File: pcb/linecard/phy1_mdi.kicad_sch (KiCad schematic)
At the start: 51 parts, among them J5 LPJT476156AENL, J9 LPJT476156AENL, U35 VSC8512, U36 ESD224DQAR, U37 ESD224DQAR, U38 ESD224DQAR, U39 ESD224DQAR, U40 ESD224DQAR, U41 ESD224DQAR, U42 ESD224DQAR, U43 ESD224DQAR, U44 ESD224DQAR, U45 ESD224DQAR, U46 ESD224DQAR, U47 ESD224DQAR, U48 ESD224DQAR, U49 ESD224DQAR, U50 ESD224DQAR, U51 ESD224DQAR, U52 ESD224DQAR, U53 ESD224DQAR, U54 ESD224DQAR, U55 ESD224DQAR, U56 ESD224DQAR, U57 ESD224DQAR, U58 ESD224DQAR, U59 ESD224DQAR

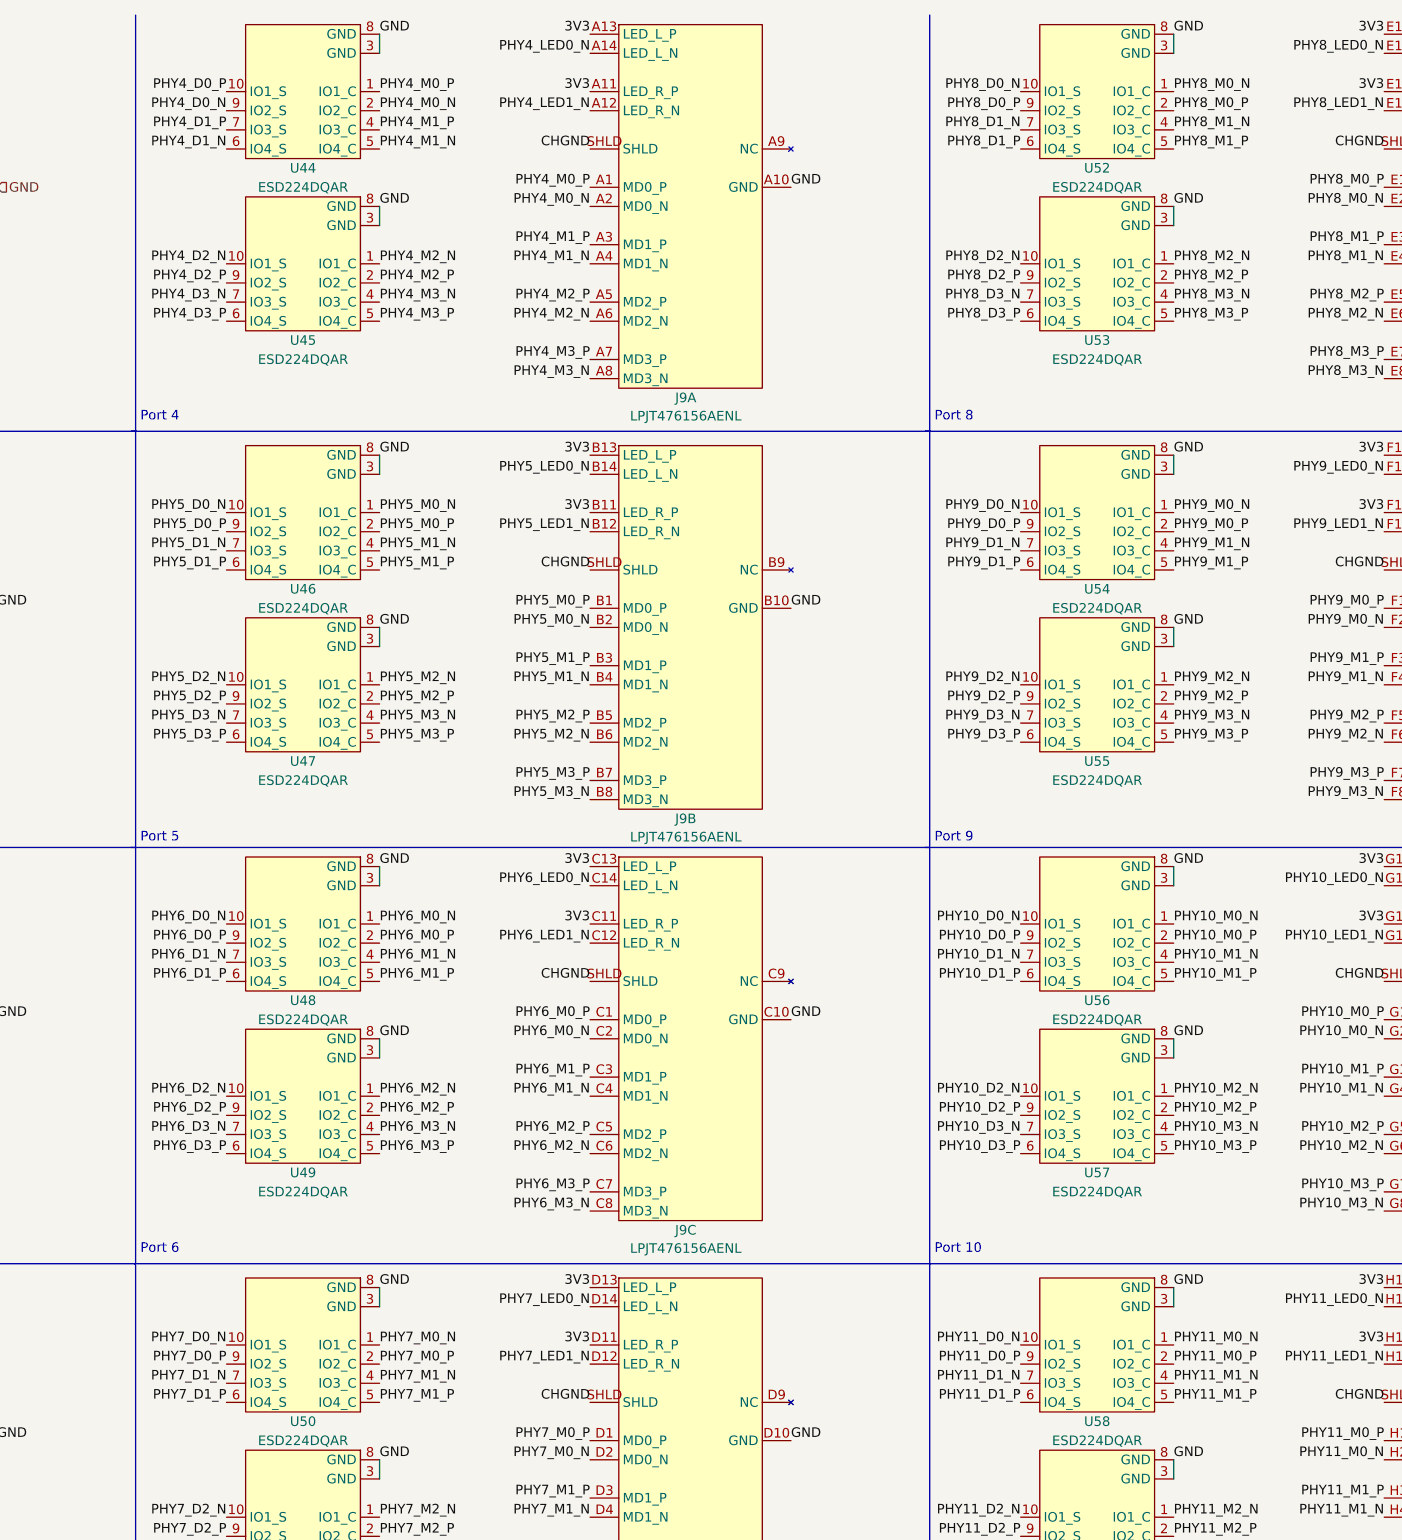
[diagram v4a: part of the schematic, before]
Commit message: 576 unrouted. More decoupling and baseT work on right side PHY. Started LED fanout.
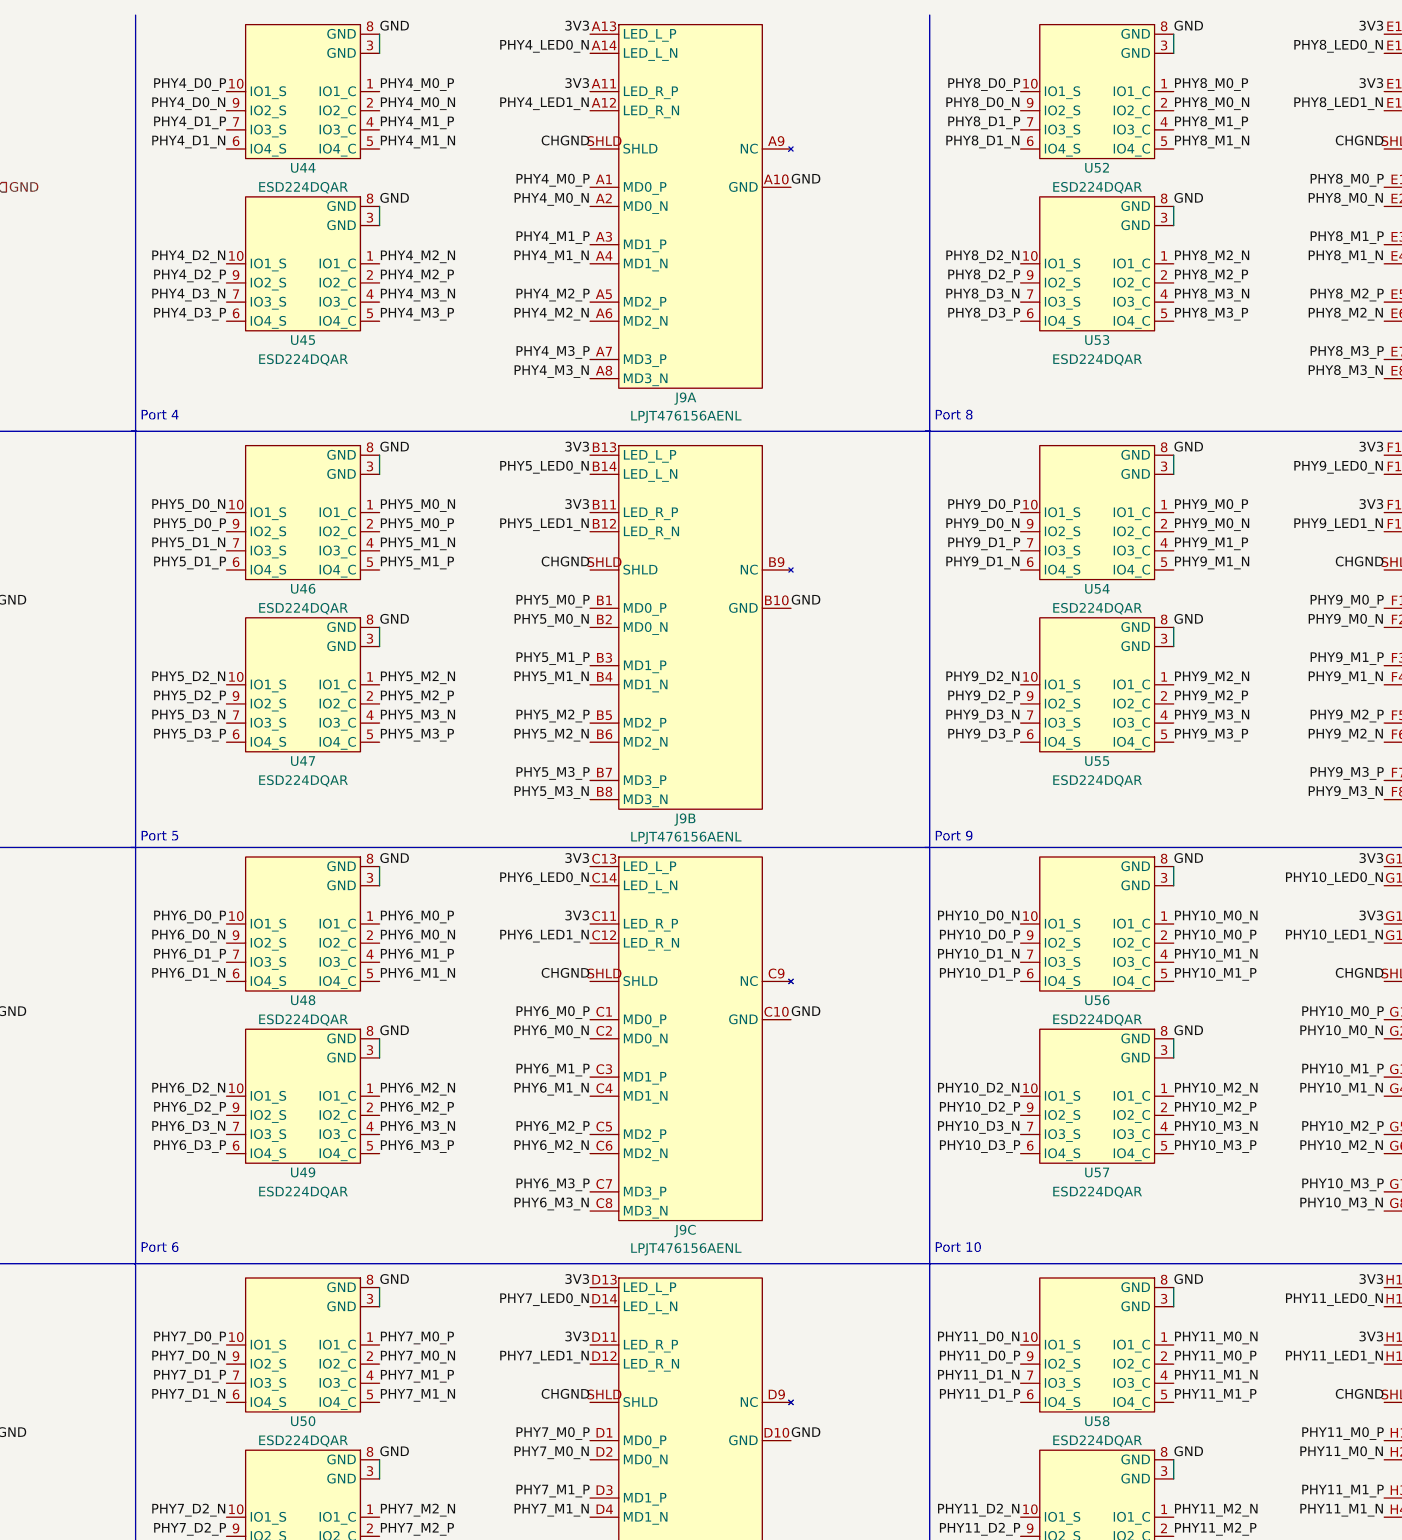
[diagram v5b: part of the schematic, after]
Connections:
- net PHY6_D0_N: now also U48.9 (IO2_S); no longer U48.10 (IO1_S)
- net PHY6_D0_P: now also U48.10 (IO1_S); no longer U48.9 (IO2_S)
- net PHY6_D1_N: now also U48.6 (IO4_S); no longer U48.7 (IO3_S)
- net PHY6_D1_P: now also U48.7 (IO3_S); no longer U48.6 (IO4_S)
- net PHY6_M0_N: now also U48.2 (IO2_C); no longer U48.1 (IO1_C)
- net PHY6_M0_P: now also U48.1 (IO1_C); no longer U48.2 (IO2_C)
- net PHY6_M1_N: now also U48.5 (IO4_C); no longer U48.4 (IO3_C)
- net PHY6_M1_P: now also U48.4 (IO3_C); no longer U48.5 (IO4_C)
- net PHY7_D0_N: now also U50.9 (IO2_S); no longer U50.10 (IO1_S)
- net PHY7_D0_P: now also U50.10 (IO1_S); no longer U50.9 (IO2_S)
- net PHY7_D1_N: now also U50.6 (IO4_S); no longer U50.7 (IO3_S)
- net PHY7_D1_P: now also U50.7 (IO3_S); no longer U50.6 (IO4_S)
- net PHY7_M0_N: now also U50.2 (IO2_C); no longer U50.1 (IO1_C)
- net PHY7_M0_P: now also U50.1 (IO1_C); no longer U50.2 (IO2_C)
- net PHY7_M1_N: now also U50.5 (IO4_C); no longer U50.4 (IO3_C)
- net PHY7_M1_P: now also U50.4 (IO3_C); no longer U50.5 (IO4_C)
- net PHY8_D0_N: now also U52.9 (IO2_S); no longer U52.10 (IO1_S)
- net PHY8_D0_P: now also U52.10 (IO1_S); no longer U52.9 (IO2_S)
- net PHY8_D1_N: now also U52.6 (IO4_S); no longer U52.7 (IO3_S)
- net PHY8_D1_P: now also U52.7 (IO3_S); no longer U52.6 (IO4_S)
- net PHY8_M0_N: now also U52.2 (IO2_C); no longer U52.1 (IO1_C)
- net PHY8_M0_P: now also U52.1 (IO1_C); no longer U52.2 (IO2_C)
- net PHY8_M1_N: now also U52.5 (IO4_C); no longer U52.4 (IO3_C)
- net PHY8_M1_P: now also U52.4 (IO3_C); no longer U52.5 (IO4_C)
- net PHY9_D0_N: now also U54.9 (IO2_S); no longer U54.10 (IO1_S)
- net PHY9_D0_P: now also U54.10 (IO1_S); no longer U54.9 (IO2_S)
- net PHY9_D1_N: now also U54.6 (IO4_S); no longer U54.7 (IO3_S)
- net PHY9_D1_P: now also U54.7 (IO3_S); no longer U54.6 (IO4_S)
- net PHY9_M0_N: now also U54.2 (IO2_C); no longer U54.1 (IO1_C)
- net PHY9_M0_P: now also U54.1 (IO1_C); no longer U54.2 (IO2_C)
- net PHY9_M1_N: now also U54.5 (IO4_C); no longer U54.4 (IO3_C)
- net PHY9_M1_P: now also U54.4 (IO3_C); no longer U54.5 (IO4_C)
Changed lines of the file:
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@@
 	)
 	(label "PHY6_M1_P"
-		(at 228.6 140.97 0)
+		(at 228.6 138.43 0)
 		(fields_autoplaced yes)
 		(effects
@@
 	)
 	(label "PHY8_D1_P"
-		(at 313.69 30.48 180)
+		(at 313.69 27.94 180)
 		(fields_autoplaced yes)
 		(effects
@@
 	)
 	(label "PHY8_D1_N"
-		(at 313.69 27.94 180)
+		(at 313.69 30.48 180)
 		(fields_autoplaced yes)
 		(effects
@@
 	)
 	(label "PHY9_M0_N"
-		(at 334.01 78.74 0)
+		(at 334.01 81.28 0)
 		(fields_autoplaced yes)
 		(effects
@@
 	)
 	(label "PHY7_D0_N"
-		(at 208.28 189.23 180)
+		(at 208.28 191.77 180)
 		(fields_autoplaced yes)
 		(effects
@@
 	)
 	(label "PHY7_D0_P"
-		(at 208.28 191.77 180)
+		(at 208.28 189.23 180)
 		(fields_autoplaced yes)
 		(effects
@@
 	)
 	(label "PHY9_D0_N"
-		(at 313.69 78.74 180)
+		(at 313.69 81.28 180)
 		(fields_autoplaced yes)
 		(effects
@@
 	)
 	(label "PHY8_M0_P"
-		(at 334.01 25.4 0)
+		(at 334.01 22.86 0)
 		(fields_autoplaced yes)
 		(effects
@@
 	)
 	(label "PHY9_D1_N"
-		(at 313.69 83.82 180)
+		(at 313.69 86.36 180)
 		(fields_autoplaced yes)
 		(effects
@@
 	)
 	(label "PHY9_D1_P"
-		(at 313.69 86.36 180)
+		(at 313.69 83.82 180)
 		(fields_autoplaced yes)
 		(effects
@@
 	)
 	(label "PHY6_D1_P"
-		(at 208.28 140.97 180)
+		(at 208.28 138.43 180)
 		(fields_autoplaced yes)
 		(effects
@@
 	)
 	(label "PHY9_M0_P"
-		(at 334.01 81.28 0)
+		(at 334.01 78.74 0)
 		(fields_autoplaced yes)
 		(effects
@@
 	)
 	(label "PHY8_M1_N"
-		(at 334.01 27.94 0)
+		(at 334.01 30.48 0)
 		(fields_autoplaced yes)
 		(effects
@@
 	)
 	(label "PHY8_D0_P"
-		(at 313.69 25.4 180)
+		(at 313.69 22.86 180)
 		(fields_autoplaced yes)
 		(effects
@@
 	)
 	(label "PHY6_M0_P"
-		(at 228.6 135.89 0)
+		(at 228.6 133.35 0)
 		(fields_autoplaced yes)
 		(effects
@@
 	)
 	(label "PHY7_M1_N"
-		(at 228.6 194.31 0)
+		(at 228.6 196.85 0)
 		(fields_autoplaced yes)
 		(effects
@@
 	)
 	(label "PHY9_D0_P"
-		(at 313.69 81.28 180)
+		(at 313.69 78.74 180)
 		(fields_autoplaced yes)
 		(effects
@@
 	)
 	(label "PHY6_M0_N"
-		(at 228.6 133.35 0)
+		(at 228.6 135.89 0)
 		(fields_autoplaced yes)
 		(effects
@@
 	)
 	(label "PHY7_M0_P"
-		(at 228.6 191.77 0)
+		(at 228.6 189.23 0)
 		(fields_autoplaced yes)
 		(effects
@@
 	)
 	(label "PHY6_M1_N"
-		(at 228.6 138.43 0)
+		(at 228.6 140.97 0)
 		(fields_autoplaced yes)
 		(effects
@@
 	)
 	(label "PHY7_M1_P"
-		(at 228.6 196.85 0)
+		(at 228.6 194.31 0)
 		(fields_autoplaced yes)
 		(effects
@@
 	)
 	(label "PHY9_M1_N"
-		(at 334.01 83.82 0)
+		(at 334.01 86.36 0)
 		(fields_autoplaced yes)
 		(effects
@@
 	)
 	(label "PHY8_M1_P"
-		(at 334.01 30.48 0)
+		(at 334.01 27.94 0)
 		(fields_autoplaced yes)
 		(effects
@@
 	)
 	(label "PHY6_D0_N"
-		(at 208.28 133.35 180)
+		(at 208.28 135.89 180)
 		(fields_autoplaced yes)
 		(effects
@@
 	)
 	(label "PHY6_D0_P"
-		(at 208.28 135.89 180)
+		(at 208.28 133.35 180)
 		(fields_autoplaced yes)
 		(effects
@@
 	)
 	(label "PHY7_D1_N"
-		(at 208.28 194.31 180)
+		(at 208.28 196.85 180)
 		(fields_autoplaced yes)
 		(effects
@@
 	)
 	(label "PHY8_D0_N"
-		(at 313.69 22.86 180)
+		(at 313.69 25.4 180)
 		(fields_autoplaced yes)
 		(effects
@@
 	)
 	(label "PHY8_M0_N"
-		(at 334.01 22.86 0)
+		(at 334.01 25.4 0)
 		(fields_autoplaced yes)
 		(effects
@@
 	)
 	(label "PHY6_D1_N"
-		(at 208.28 138.43 180)
+		(at 208.28 140.97 180)
 		(fields_autoplaced yes)
 		(effects
@@
 	)
 	(label "PHY7_D1_P"
-		(at 208.28 196.85 180)
+		(at 208.28 194.31 180)
 		(fields_autoplaced yes)
 		(effects
@@
 	)
 	(label "PHY7_M0_N"
-		(at 228.6 189.23 0)
+		(at 228.6 191.77 0)
 		(fields_autoplaced yes)
 		(effects
@@
 	)
 	(label "PHY9_M1_P"
-		(at 334.01 86.36 0)
+		(at 334.01 83.82 0)
 		(fields_autoplaced yes)
 		(effects
